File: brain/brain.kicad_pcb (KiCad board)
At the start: 2 copper layers, 100 x 80 mm, 221 parts, among them U1 TXB0108, U10 TSR1-2433, U2 74HC154, U3 TXB0108, U4 TXB0108, U5 PCA9306, U6 PCA9685, U7 TXB0108, U8 STM32F407VG, U9 TSR1-2450, Y1 8M

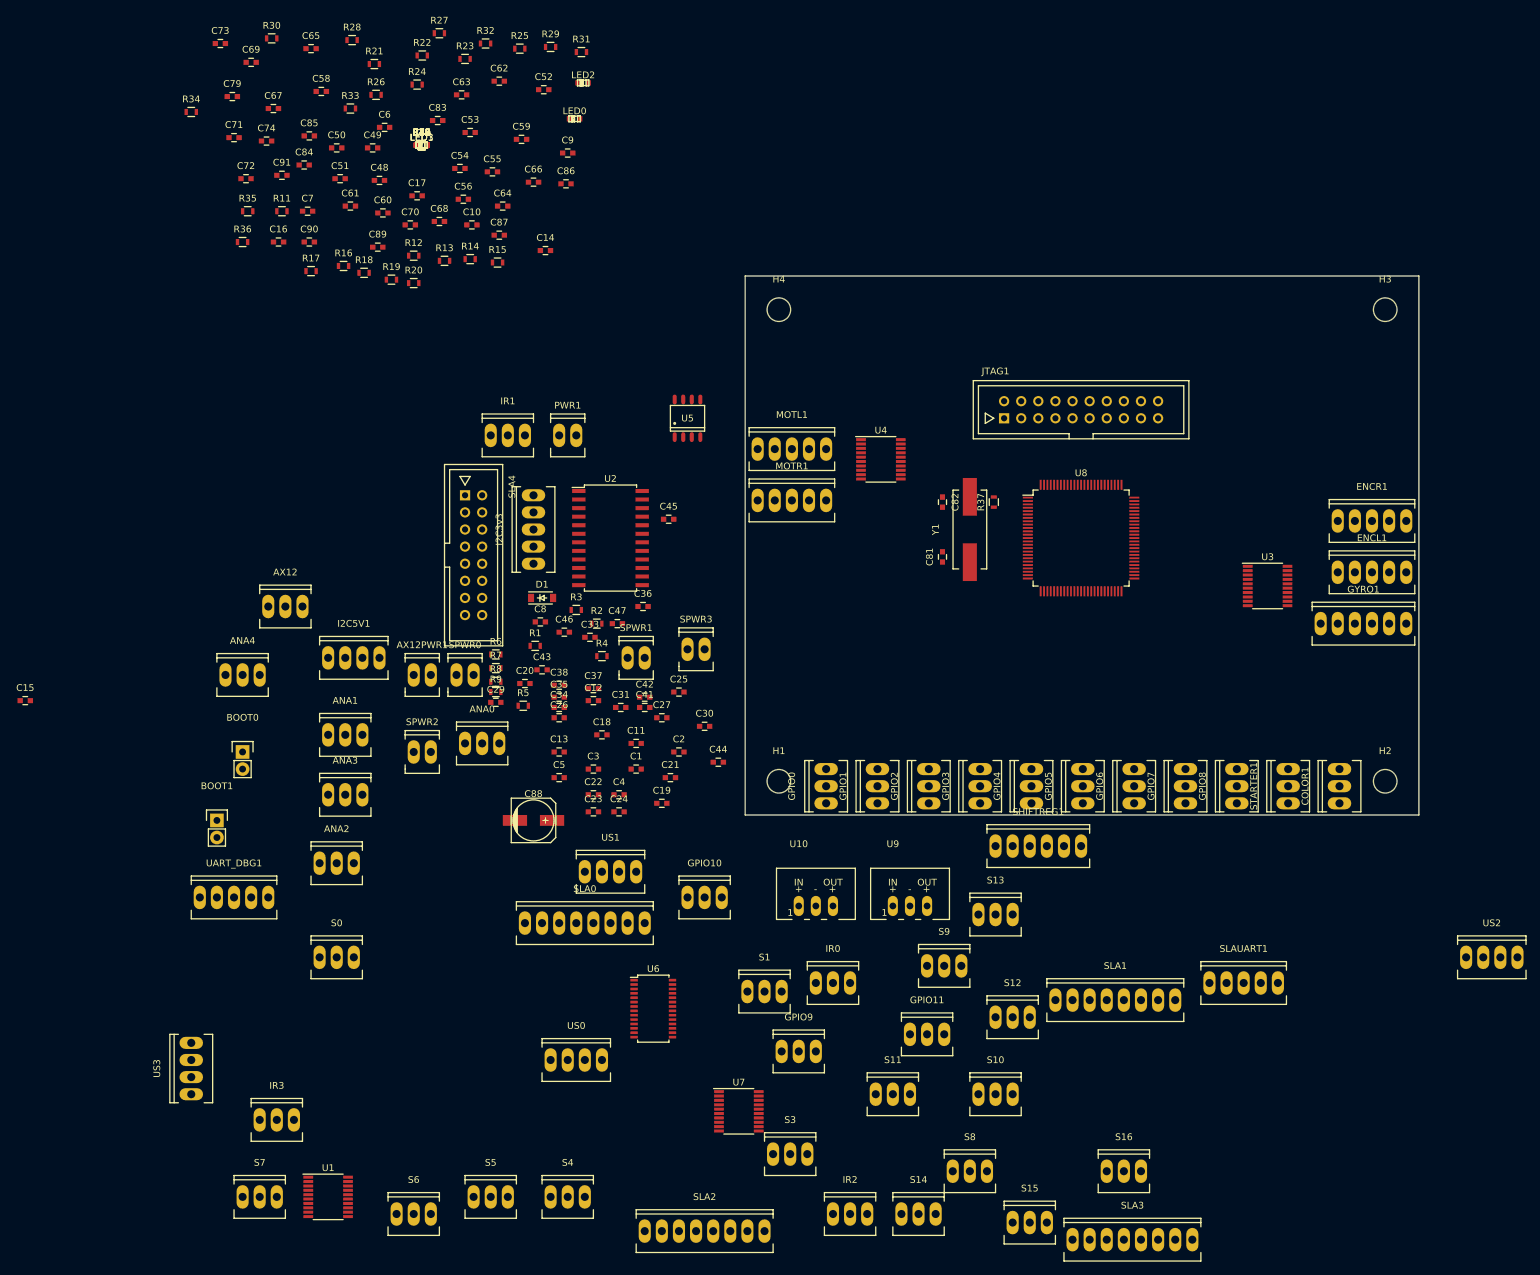
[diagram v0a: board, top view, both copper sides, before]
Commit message: all tracks are routed
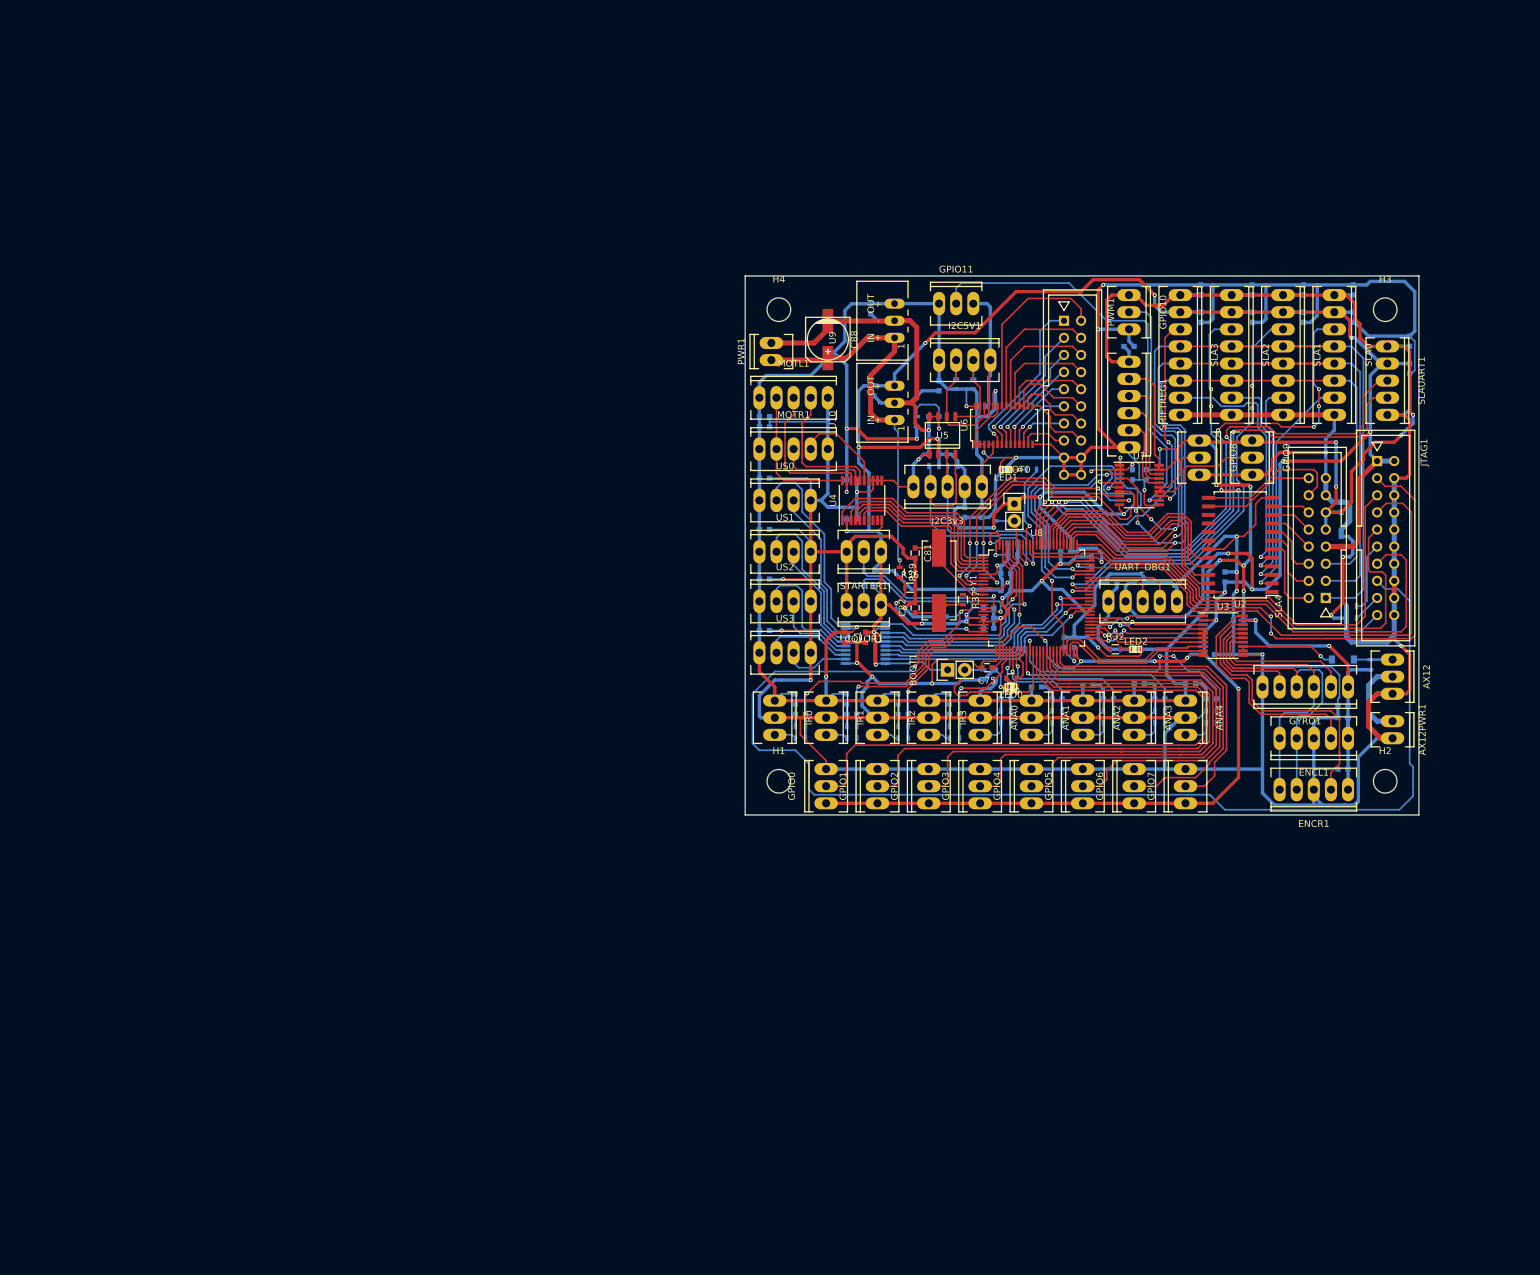
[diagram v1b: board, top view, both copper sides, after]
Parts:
- removed C35, C36, C37, C38, C42, C43, C44, C45, C48, C49, C50, C51, C53, C54, C55, C56: 4u7, Capacitors_SMD:C_0603
- removed LED3: LED, LEDs:LED-0603
- removed R13, R14, R16, R9: NC, Resistors_SMD:R_0603
- removed R33: 220, Resistors_SMD:R_0603
- removed S0, S1, S10, S11, S12, S13, S14, S15, S16, S3, S4, S5, S6, S7, S8, S9: CONN_3, Sockets_MOLEX_KK-System:Socket_MOLEX-KK-RM2-54mm_Lock_3pin_straight
- removed SPWR0, SPWR1, SPWR2, SPWR3: CONN_2, Sockets_MOLEX_KK-System:Socket_MOLEX-KK-RM2-54mm_Lock_2pin_straight
- added PWM1: HE10-20, espitall:HE10_20D, F.Cu at (148.6, 68.1)
- C10, C11, C12, C13, C14, C15, C16, C17, C18, C19, C20, C21, C22, C23, C24, C25, C26, C27, C28, C29, C3, C30, C31, C32, C33, C34, C39, C4, C40, C41, C46, C47, C5, C52, C57, C58, C59, C6, C60, C61, C62, C63, C64, C65, C66, C67, C68, C69, C7, C70, C71, C72, C73, C74, C76, C77, C78, C79, C8, C80, C83, C84, C85, C86, C87, C89, C9, C90, C91, D1, R1, R10, R11, R12, R15, R17, R18, R19, R2, R20, R21, R22, R23, R24, R25, R26, R27, R28, R3, R31, R34, R35, R38, R39, R4, R40, R41, R42, R5, R6, R7, R8, U1: moved to B.Cu
- moved C15 179.0 mm to (171.2, 94.7), turned to 90 degrees
- moved C91 169.8 mm to (198.6, 63.8), turned to 270 degrees
- moved C69 164.7 mm to (161.5, 112.8), turned to 180 degrees
- moved AX12 164.7 mm to (196.1, 109.5), turned to 270 degrees
- moved C90 164.0 mm to (198.6, 59.7), turned to 90 degrees
- moved C16 159.9 mm to (190.2, 56.1), turned to 270 degrees
- moved R28 155.8 mm to (161.5, 114.6), turned to 180 degrees
- moved R40 155.6 mm to (190.0, 102.6), turned to 180 degrees
- moved R41 154.8 mm to (190.0, 100.8), turned to 180 degrees
- moved R42 154.0 mm to (190.0, 99.0), turned to 180 degrees
- moved C67 151.8 mm to (153.9, 112.8), turned to 180 degrees
- moved SLA2 151.8 mm to (172.2, 61.7), turned to 270 degrees
- moved R27 148.0 mm to (161.5, 116.3)
- moved C65 146.9 mm to (146.3, 112.8), turned to 180 degrees
- moved R30 145.1 mm to (139.4, 109.7), turned to 180 degrees
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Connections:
- SLA2 pad 6: /Slave/SLA_SPI_CS1_3v3 -> /GPIO/SLA_SPI_SCK_3v3
- SLA3 pad 6: /Slave/SLA_SPI_CS1_3v3 -> /GPIO/SLA_SPI_SCK_3v3
- SLA4 pad 5: /Slave/SLA_SPI_CS1_3v3 -> /GPIO/SLA_SPI_SCK_3v3
- U6 pad 10: /Servo/S4_5V -> Net-(PWM1-Pad9)
- U6 pad 11: /Servo/S5_5V -> Net-(PWM1-Pad11)
- U6 pad 12: /Servo/S6_5V -> Net-(PWM1-Pad13)
- U6 pad 13: /Servo/S7_5V -> Net-(PWM1-Pad15)
- U6 pad 15: /Servo/S8_5V -> Net-(PWM1-Pad16)
- U6 pad 16: /Servo/S9_5V -> Net-(PWM1-Pad14)
- U6 pad 17: /Servo/S10_5V -> Net-(PWM1-Pad12)
- U6 pad 18: /Servo/S11_5V -> Net-(PWM1-Pad10)
- U6 pad 19: /Servo/S12_5V -> Net-(PWM1-Pad8)
- U6 pad 20: /Servo/S13_5V -> Net-(PWM1-Pad6)
- U6 pad 21: /Servo/S14_5V -> Net-(PWM1-Pad4)
- U6 pad 22: /Servo/S15_5V -> Net-(PWM1-Pad2)
- U6 pad 6: /Servo/S0_5V -> Net-(PWM1-Pad1)
- U6 pad 7: /Servo/S1_5V -> Net-(PWM1-Pad3)
- U6 pad 8: /Servo/S2_5V -> Net-(PWM1-Pad5)
- U6 pad 9: /Servo/S3_5V -> Net-(PWM1-Pad7)
- U8 pad 15: /GPIO/GPIO9_3v3 -> Net-(U8-Pad15)
- U8 pad 16: /GPIO/GPIO10_3v3 -> /GPIO/STARTER_3v3
- U8 pad 17: /GPIO/GPIO11_3v3 -> /GPIO/COLOR_3v3
- U8 pad 33: Net-(U8-Pad33) -> /uc/LED0_3v3
- U8 pad 58: /uc/LED3_3v3 -> Net-(U8-Pad58)
- U8 pad 67: /uc/LED0_3v3 -> Net-(U8-Pad67)
- U8 pad 7: Net-(U8-Pad7) -> /GPIO/GPIO9_3v3
- U8 pad 8: /GPIO/STARTER_3v3 -> /GPIO/GPIO10_3v3
- U8 pad 9: /GPIO/COLOR_3v3 -> /GPIO/GPIO11_3v3
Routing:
- net GND: track 0.00 -> 1283.3 mm, vias 0 -> 31
- net +5V: track 0.00 -> 702.1 mm, vias 0 -> 19
- net +3V3: track 0.00 -> 653.4 mm, vias 0 -> 31
- net /uc/nSRST_3v3: track 0.00 -> 192.8 mm, vias 0 -> 2
- net /GPIO/SLA_SPI_MOSI_3v3: track 0.00 -> 150.8 mm, vias 0 -> 2
- net /Slave/SLA_SPI_MISO_3v3: track 0.00 -> 129.8 mm, vias 0 -> 1
- net /GPIO/SLA_SPI_SCK_3v3: track 0.00 -> 126.1 mm, vias 0 -> 4
- net /GPIO/GPIO0_3v3: track 0.00 -> 97.0 mm
- net /uc/nTRST_3v3: track 0.00 -> 93.8 mm, vias 0 -> 2
- net /GPIO/GPIO1_3v3: track 0.00 -> 89.8 mm
- net /GPIO/GPIO2_3v3: track 0.00 -> 83.0 mm
- net /Slave/SLA_ALERT0_3v3: track 0.00 -> 81.6 mm, vias 0 -> 5
- net /Slave/SLA_TX_3v3: track 0.00 -> 80.8 mm, vias 0 -> 2
- net /Slave/SLA_RX_3v3: track 0.00 -> 79.8 mm, vias 0 -> 2
- net /uc/TDO_3v3: track 0.00 -> 78.0 mm
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
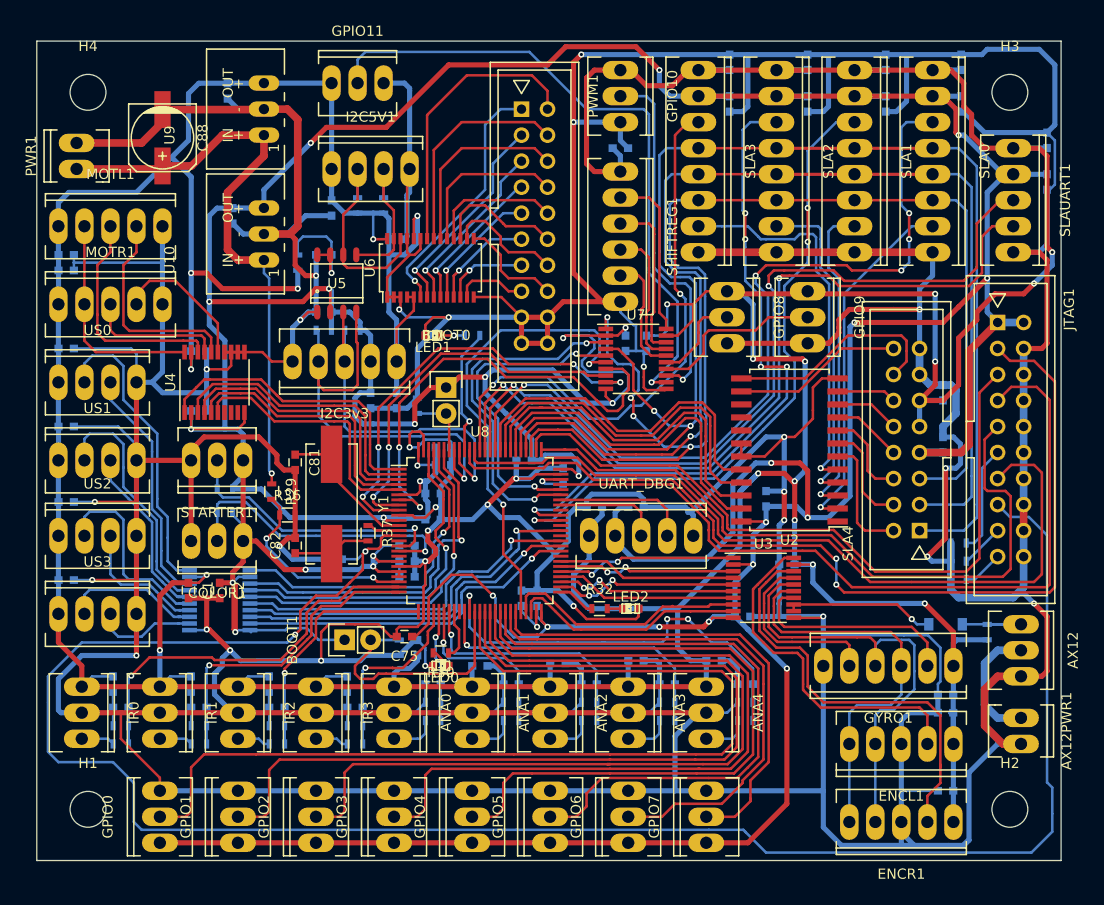
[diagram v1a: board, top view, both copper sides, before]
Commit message: add polygon pours
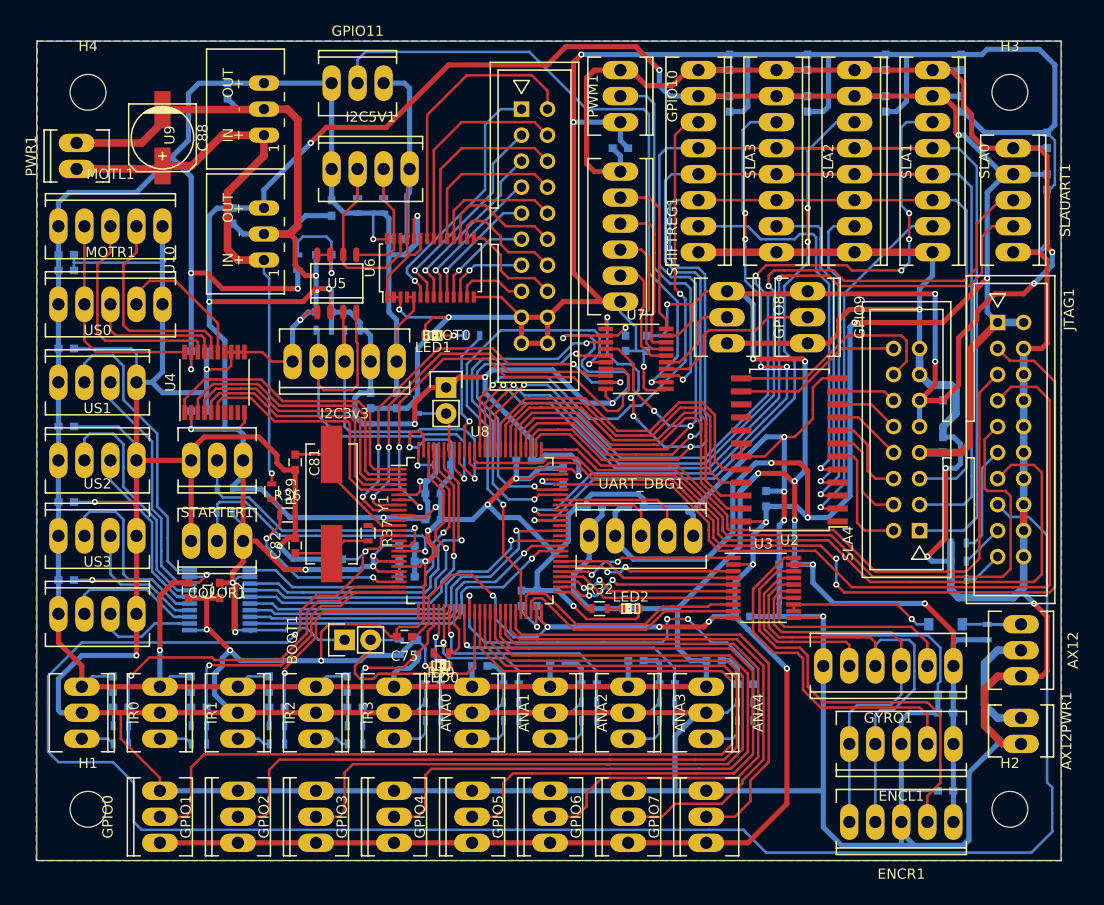
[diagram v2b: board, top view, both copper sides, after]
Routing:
- added copper zone on B.Cu, net GND
- added copper zone on F.Cu, net GND
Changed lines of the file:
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@@
   (segment (start 141.986 53.34) (end 148.336 53.34) (width 0.25) (layer F.Cu) (net 172))
   (segment (start 138.105 57.221) (end 141.986 53.34) (width 0.25) (layer F.Cu) (net 172))
+  (zone (net 2) (net_name GND) (layer F.Cu) (hatch edge 0.508)
+    (connect_pads yes (clearance 0.508))
+    (min_thickness 0.254)
+    (fill yes (arc_segments 16) (thermal_gap 0.508) (thermal_bridge_width 0.508))
+    (polygon
+      (pts
+        (xy 100.032 50.006) (xy 200.032 50.006) (xy 200.032 130.006) (xy 99.932 130.006)
+      )
+    )
+  )
+  (zone (net 2) (net_name GND) (layer B.Cu) (hatch edge 0.508)
+    (connect_pads yes (clearance 0.508))
+    (min_thickness 0.254)
+    (fill yes (arc_segments 16) (thermal_gap 0.508) (thermal_bridge_width 0.508))
+    (polygon
+      (pts
+        (xy 100.032 50.006) (xy 200.032 50.006) (xy 200.032 130.006) (xy 99.932 130.006)
+      )
+    )
+  )
 )

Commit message: silkscreen. Board ready for production
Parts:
- renumbered AX12PWR1 to AX12PWR, COLOR1 to COLOR, ENCL1 to ENCL, ENCR1 to ENCR, GYRO1 to GYRO, I2C5V1 to I2C5V, JTAG1 to JTAG, MOTL1 to MOTL, MOTR1 to MOTR, PWM1 to PWM, PWR1 to PWR, SHIFTREG1 to SHIFTREG, SLAUART1 to SLAUART, STARTER1 to STARTER, UART_DBG1 to UART_DBG
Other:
- board text added: "3v3"
- board text added: "5V"
- board text added: "ANA"
- board text added: "Brain Eurobot 2016 ~espitall"
- board text added: "GND"
- board text added: "IO"
